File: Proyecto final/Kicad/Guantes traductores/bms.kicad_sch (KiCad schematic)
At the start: 3 parts, among them U7 TP4056 Board

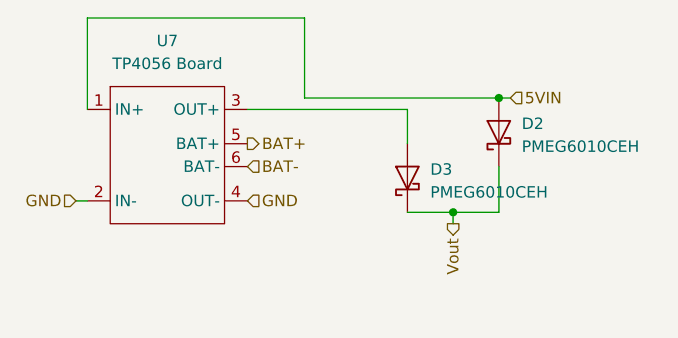
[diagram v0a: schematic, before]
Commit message: Posicion de componentes
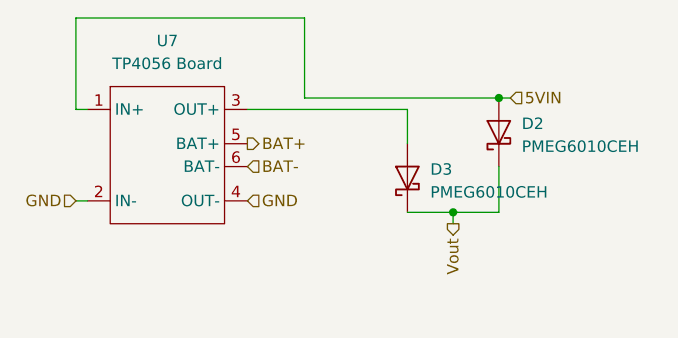
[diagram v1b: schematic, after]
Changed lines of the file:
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@@
 (kicad_sch
-	(version 20250114)
+	(version 20260306)
 	(generator "eeschema")
-	(generator_version "9.0")
+	(generator_version "10.0")
 	(paper "A4")
 	(junction
@@
 	(wire
 		(pts
-			(xy 96.52 69.85) (xy 72.39 69.85)
+			(xy 96.52 69.85) (xy 71.12 69.85)
 		)
 		(stroke
@@
 	(wire
 		(pts
+			(xy 71.12 80.01) (xy 72.39 80.01)
+		)
+		(stroke
+			(width 0)
+			(type default)
+		)
+	)
+	(wire
+		(pts
 			(xy 96.52 78.74) (xy 96.52 69.85)
 		)
@@
 	(wire
 		(pts
-			(xy 72.39 69.85) (xy 72.39 80.01)
+			(xy 71.12 69.85) (xy 71.12 80.01)
 		)
 		(stroke
@@
 		(at 74.93 77.47 0)
 		(unit 1)
+		(body_style 1)
 		(exclude_from_sim no)
 		(in_bom yes)
 		(on_board yes)
+		(in_pos_files yes)
 		(dnp no)
 		(fields_autoplaced yes)
 		(property "Reference" "U7"
 			(at 81.28 72.39 0)
+			(show_name no)
+			(do_not_autoplace no)
 			(effects
 				(font
@@
 		(property "Value" "TP4056 Board"
 			(at 81.28 74.93 0)
+			(show_name no)
+			(do_not_autoplace no)
 			(effects
 				(font
@@
 		(property "Footprint" "Custom board:TP4056 Board"
 			(at 74.93 77.47 0)
-			(effects
-				(font
-					(size 1.27 1.27)
-				)
-				(hide yes)
+			(hide yes)
+			(show_name no)
+			(do_not_autoplace no)
+			(effects
+				(font
+					(size 1.27 1.27)
+				)
 			)
 		)
 		(property "Datasheet" ""
 			(at 74.93 77.47 0)
-			(effects
-				(font
-					(size 1.27 1.27)
-				)
-				(hide yes)
+			(hide yes)
+			(show_name no)
+			(do_not_autoplace no)
+			(effects
+				(font
+					(size 1.27 1.27)
+				)
 			)
 		)
 		(property "Description" "External TP4056 board 5V 1A"
 			(at 83.566 76.454 0)
-			(effects
-				(font
-					(size 1.27 1.27)
-				)
-				(hide yes)
+			(hide yes)
+			(show_name no)
+			(do_not_autoplace no)
+			(effects
+				(font
+					(size 1.27 1.27)
+				)
 			)
 		)
@@
 		(at 107.95 87.63 90)
 		(unit 1)
+		(body_style 1)
 		(exclude_from_sim no)
 		(in_bom yes)
 		(on_board yes)
+		(in_pos_files yes)
 		(dnp no)
 		(fields_autoplaced yes)
 		(property "Reference" "D3"
 			(at 110.49 86.6774 90)
+			(show_name no)
+			(do_not_autoplace no)
 			(effects
 				(font
@@
 		(property "Value" "PMEG6010CEH"
 			(at 110.49 89.2174 90)
+			(show_name no)
+			(do_not_autoplace no)
 			(effects
 				(font
@@
 		(property "Footprint" "Diode_SMD:D_SOD-123F"
 			(at 112.395 87.63 0)
-			(effects
-				(font
-					(size 1.27 1.27)
-				)
-				(hide yes)
+			(hide yes)
+			(show_name no)
+			(do_not_autoplace no)
+			(effects
+				(font
+					(size 1.27 1.27)
+				)
 			)
 		)
 		(property "Datasheet" "https://assets.nexperia.com/documents/data-sheet/PMEG6010CEH_PMEG6010CEJ.pdf"
 			(at 107.95 87.63 0)
-			(effects
-				(font
-					(size 1.27 1.27)
-				)
-				(hide yes)
+			(hide yes)
+			(show_name no)
+			(do_not_autoplace no)
+			(effects
+				(font
+					(size 1.27 1.27)
+				)
 			)
 		)
 		(property "Description" "60V, 1A very low Vf MEGA Schottky barrier rectifier, SOD-123F"
 			(at 107.95 87.63 0)
-			(effects
-				(font
-					(size 1.27 1.27)
-				)
-				(hide yes)
+			(hide yes)
+			(show_name no)
+			(do_not_autoplace no)
+			(effects
+				(font
+					(size 1.27 1.27)
+				)
 			)
 		)
@@
 		(at 118.11 82.55 90)
 		(unit 1)
+		(body_style 1)
 		(exclude_from_sim no)
 		(in_bom yes)
 		(on_board yes)
+		(in_pos_files yes)
 		(dnp no)
 		(fields_autoplaced yes)
 		(property "Reference" "D2"
 			(at 120.65 81.5974 90)
+			(show_name no)
+			(do_not_autoplace no)
 			(effects
 				(font
@@
 		(property "Value" "PMEG6010CEH"
 			(at 120.65 84.1374 90)
+			(show_name no)
+			(do_not_autoplace no)
 			(effects
 				(font
@@
 		(property "Footprint" "Diode_SMD:D_SOD-123F"
 			(at 122.555 82.55 0)
-			(effects
-				(font
-					(size 1.27 1.27)
-				)
-				(hide yes)
+			(hide yes)
+			(show_name no)
+			(do_not_autoplace no)
+			(effects
+				(font
+					(size 1.27 1.27)
+				)
 			)
 		)
 		(property "Datasheet" "https://assets.nexperia.com/documents/data-sheet/PMEG6010CEH_PMEG6010CEJ.pdf"
 			(at 118.11 82.55 0)
-			(effects
-				(font
-					(size 1.27 1.27)
-				)
-				(hide yes)
+			(hide yes)
+			(show_name no)
+			(do_not_autoplace no)
+			(effects
+				(font
+					(size 1.27 1.27)
+				)
 			)
 		)
 		(property "Description" "60V, 1A very low Vf MEGA Schottky barrier rectifier, SOD-123F"
 			(at 118.11 82.55 0)
-			(effects
-				(font
-					(size 1.27 1.27)
-				)
-				(hide yes)
-			)
-		)
+			(hide yes)
+			(show_name no)
+			(do_not_autoplace no)
+			(effects
+				(font
+					(size 1.27 1.27)
+				)
+			)
+		)

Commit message: Switch y leds
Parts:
- added U6: SS12D10G5, lcsc_footprints:C7431054_SW-TH_SHOU-HAN_SS12D10G4, symbol lcsc_imported:SS12D10G5
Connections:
- net Vout: now also U6.1; no longer D2.1 (K), D3.1 (K)
- new net: D2.1 (K), D3.1 (K), U6.2
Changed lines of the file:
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@@
+	(wire
+		(pts
+			(xy 71.12 90.17) (xy 72.39 90.17)
+		)
+		(stroke
+			(width 0)
+			(type default)
+		)
+	)
+	(wire
+		(pts
+			(xy 115.57 95.25) (xy 118.11 95.25)
+		)
+		(stroke
+			(width 0)
+			(type default)
+		)
+	)
+	(wire
+		(pts
+			(xy 113.03 91.44) (xy 113.03 95.25)
+		)
+		(stroke
+			(width 0)
+			(type default)
+		)
+	)
+	(wire
+		(pts
+			(xy 96.52 78.74) (xy 118.11 78.74)
+		)
+		(stroke
+			(width 0)
+			(type default)
+		)
+	)
 	(wire
 		(pts
@@
 	(wire
 		(pts
-			(xy 71.12 90.17) (xy 72.39 90.17)
-		)
-		(stroke
-			(width 0)
-			(type default)
-		)
-	)
-	(wire
-		(pts
-			(xy 113.03 91.44) (xy 113.03 92.71)
-		)
-		(stroke
-			(width 0)
-			(type default)
-		)
-	)
-	(wire
-		(pts
-			(xy 96.52 78.74) (xy 118.11 78.74)
-		)
-		(stroke
-			(width 0)
-			(type default)
-		)
-	)
-	(wire
-		(pts
 			(xy 71.12 80.01) (xy 72.39 80.01)
 		)
@@
 	(wire
 		(pts
+			(xy 107.95 91.44) (xy 113.03 91.44)
+		)
+		(stroke
+			(width 0)
+			(type default)
+		)
+	)
+	(wire
+		(pts
 			(xy 118.11 91.44) (xy 118.11 86.36)
 		)
@@
 		(pts
 			(xy 107.95 80.01) (xy 107.95 83.82)
-		)
-		(stroke
-			(width 0)
-			(type default)
-		)
-	)
-	(wire
-		(pts
-			(xy 107.95 91.44) (xy 113.03 91.44)
 		)
 		(stroke
@@
 	(hierarchical_label "Vout"
 		(shape output)
-		(at 113.03 92.71 270)
-		(effects
-			(font
-				(size 1.27 1.27)
-			)
-			(justify right)
-		)
-	)
+		(at 118.11 95.25 0)
+		(effects
+			(font
+				(size 1.27 1.27)
+			)
+			(justify left)
+		)
+	)
+	(symbol
+		(lib_id "lcsc_imported:SS12D10G5")
+		(at 113.03 98.806 180)
+		(unit 1)
+		(body_style 1)
+		(exclude_from_sim no)
+		(in_bom yes)
+		(on_board yes)
+		(in_pos_files yes)
+		(dnp no)
+		(fields_autoplaced yes)
+		(property "Reference" "U6"
+			(at 116.84 99.3139 0)
+			(show_name no)
+			(do_not_autoplace no)
+			(effects
+				(font
+					(size 1.27 1.27)
+				)
+				(justify right)
+			)
+		)
+		(property "Value" "SS12D10G5"
+			(at 116.84 101.8539 0)
+			(show_name no)
+			(do_not_autoplace no)
+			(effects
+				(font
+					(size 1.27 1.27)
+				)
+				(justify right)
+			)
+		)
+		(property "Footprint" "lcsc_footprints:C7431054_SW-TH_SHOU-HAN_SS12D10G4"
+			(at 113.03 88.646 0)
+			(hide yes)
+			(show_name no)
+			(do_not_autoplace no)
+			(effects
+				(font
+					(size 1.27 1.27)
+				)
+			)
+		)
+		(property "Datasheet" "https://wmsc.lcsc.com/wmsc/upload/file/pdf/v2/lcsc/2311301507_SHOU-HAN-SS12D10G5_C7431054.pdf"
+			(at 115.316 98.933 0)
+			(hide yes)
+			(show_name no)
+			(do_not_autoplace no)
+			(effects
+				(font
+					(size 1.27 1.27)
+				)
+			)
+		)
+		(property "Description" "SS12D10G5"
+			(at 113.03 98.806 0)
+			(hide yes)
+			(show_name no)
+			(do_not_autoplace no)
+			(effects
+				(font
+					(size 1.27 1.27)
+				)
+			)
+		)
+		(property "LCSC" "C7431054"
+			(at 113.03 98.806 0)
+			(hide yes)
+			(show_name no)
+			(do_not_autoplace no)
+			(effects
+				(font
+					(size 1.27 1.27)
+				)
+			)
+		)
+		(property "Manufacturer" "SHOU HAN(首韩)"
+			(at 113.03 98.806 0)
+			(hide yes)
+			(show_name no)
+			(do_not_autoplace no)
+			(effects
+				(font
+					(size 1.27 1.27)
+				)
+			)
+		)
+		(pin "2"
+		)
+		(pin "3"
+		)
+		(pin "1"
+		)
+		(instances
+			(project "Guantes traductores"
+				(path "/00699b90-32f8-49a9-88ac-8ba611fc0511/c4beff49-d50b-4a5c-9cf7-50a7c6760d68"
+					(reference "U6")
+					(unit 1)
+				)
+			)
+		)
+	)

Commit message: Preparacion para pedido JLCPCB
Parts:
- D2, D3: value PMEG6010CEH -> SMD26PL-TP
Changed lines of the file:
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@@
 			)
 		)
-		(property "Value" "PMEG6010CEH"
+		(property "Value" "SMD26PL-TP"
 			(at 110.49 89.2174 90)
 			(show_name no)
@@
 			)
 		)
-		(property "Value" "PMEG6010CEH"
+		(property "Value" "SMD26PL-TP"
 			(at 120.65 84.1374 90)
 			(show_name no)
